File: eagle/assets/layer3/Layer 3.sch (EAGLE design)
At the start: 84 parts, among them Q2 AO3402, X1 SM06B-SRSS-TB, Y1 8MHz

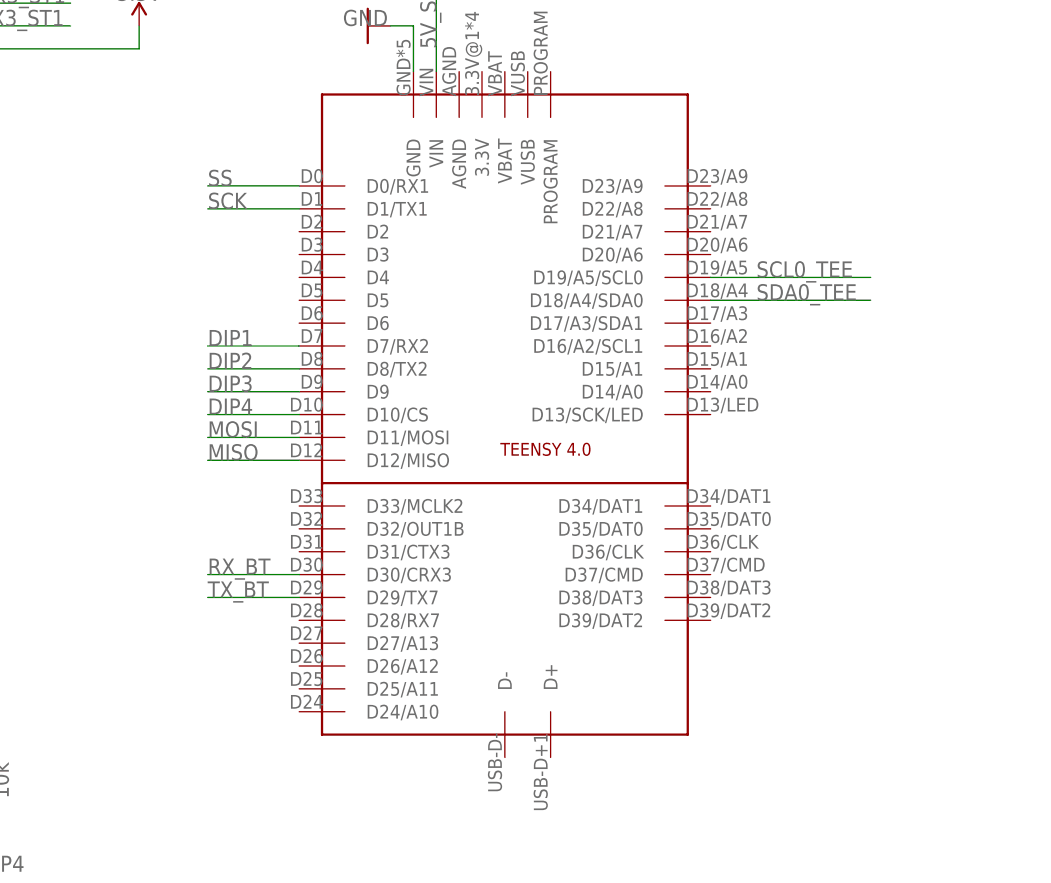
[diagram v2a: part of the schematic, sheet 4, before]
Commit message: final integration of teensy 4 to board
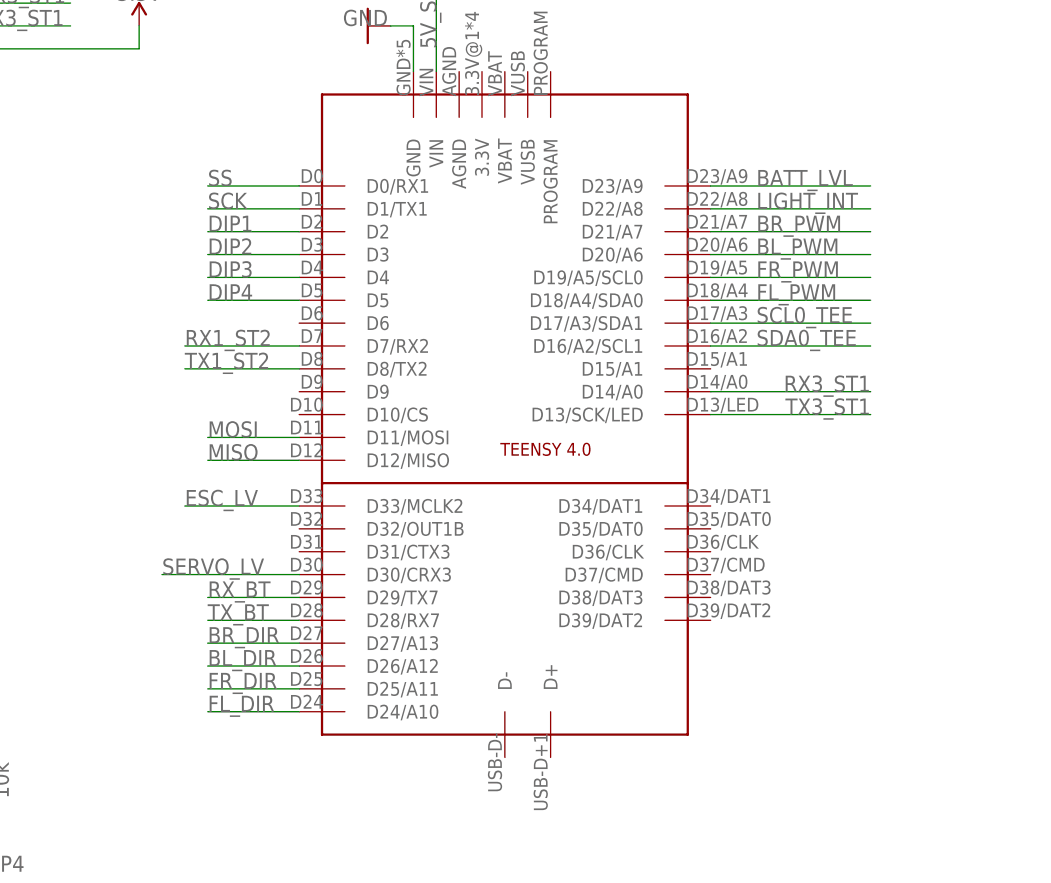
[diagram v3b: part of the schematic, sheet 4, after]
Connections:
- net BATT_LVL: now also U$1.D23/A9
- net BL_DIR: now also U$1.D26/A12
- net BL_PWM: now also U$1.D20/A6
- net BR_DIR: now also U$1.D27/A13
- net BR_PWM: now also U$1.D21/A7
- net DIP1: now also U$1.D2; no longer U$1.D7/RX2
- net DIP2: now also U$1.D3; no longer U$1.D8/TX2
- net DIP3: now also U$1.D4; no longer U$1.D9
- net DIP4: now also U$1.D5; no longer U$1.D10/CS
- net ESC_LV: now also U$1.D33/MCLK2
- net FL_DIR: now also U$1.D24/A10
- net FL_PWM: now also U$1.D18/A4/SDA0
- net FR_DIR: now also U$1.D25/A11
- net FR_PWM: now also U$1.D19/A5/SCL0
- net LIGHT_INT: now also U$1.D22/A8
- net RX1_ST2: now also U$1.D7/RX2
- net RX3_ST1: now also U$1.D14/A0
- net RX_BT: now also U$1.D29/TX7; no longer U$1.D30/CRX3
- net SCL0_TEE: now also U$1.D17/A3/SDA1; no longer U$1.D19/A5/SCL0
- net SDA0_TEE: now also U$1.D16/A2/SCL1; no longer U$1.D18/A4/SDA0
- net SERVO_LV: now also U$1.D30/CRX3
- net TX1_ST2: now also U$1.D8/TX2
- net TX3_ST1: now also U$1.D13/SCK/LED
- net TX_BT: now also U$1.D28/RX7; no longer U$1.D29/TX7
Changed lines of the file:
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@@
 <label x="48.26" y="154.94" size="1.778" layer="95"/>
+</segment>
+<segment>
+<pinref part="U$1" gate="G$1" pin="D24/A10"/>
+<wire x1="83.82" y1="66.04" x2="73.66" y2="66.04" width="0.1524" layer="91"/>
+<label x="73.66" y="66.04" size="1.778" layer="95"/>
 </segment>
 </net>
@@
 <label x="48.26" y="152.4" size="1.778" layer="95"/>
 </segment>
+<segment>
+<pinref part="U$1" gate="G$1" pin="D25/A11"/>
+<wire x1="83.82" y1="68.58" x2="73.66" y2="68.58" width="0.1524" layer="91"/>
+<label x="73.66" y="68.58" size="1.778" layer="95"/>
+</segment>
 </net>
 <net name="BL_DIR" class="0">
@@
 <label x="48.26" y="149.86" size="1.778" layer="95"/>
 </segment>
+<segment>
+<pinref part="U$1" gate="G$1" pin="D26/A12"/>
+<wire x1="83.82" y1="71.12" x2="73.66" y2="71.12" width="0.1524" layer="91"/>
+<label x="73.66" y="71.12" size="1.778" layer="95"/>
+</segment>
 </net>
 <net name="BR_DIR" class="0">
@@
 <label x="48.26" y="147.32" size="1.778" layer="95"/>
 </segment>
+<segment>
+<pinref part="U$1" gate="G$1" pin="D27/A13"/>
+<wire x1="83.82" y1="73.66" x2="73.66" y2="73.66" width="0.1524" layer="91"/>
+<label x="73.66" y="73.66" size="1.778" layer="95"/>
+</segment>
 </net>
 <net name="RX3_ST1" class="0">
@@
 <label x="48.26" y="144.78" size="1.778" layer="95"/>
 </segment>
+<segment>
+<wire x1="129.54" y1="101.6" x2="147.32" y2="101.6" width="0.1524" layer="91"/>
+<label x="147.32" y="103.378" size="1.778" layer="95" rot="R180"/>
+<pinref part="U$1" gate="G$1" pin="D14/A0"/>
+</segment>
 </net>
 <net name="TX3_ST1" class="0">
@@
 <wire x1="48.26" y1="142.24" x2="58.42" y2="142.24" width="0.1524" layer="91"/>
 <label x="48.26" y="142.24" size="1.778" layer="95"/>
+</segment>
+<segment>
+<wire x1="129.54" y1="99.06" x2="147.32" y2="99.06" width="0.1524" layer="91"/>
+<label x="147.32" y="100.838" size="1.778" layer="95" rot="R180"/>
+<pinref part="U$1" gate="G$1" pin="D13/SCK/LED"/>
 </segment>
 </net>
@@
 <label x="22.86" y="154.94" size="1.778" layer="95"/>
 </segment>
+<segment>
+<pinref part="U$1" gate="G$1" pin="D18/A4/SDA0"/>
+<wire x1="129.54" y1="111.76" x2="147.32" y2="111.76" width="0.1524" layer="91"/>
+<label x="134.62" y="111.76" size="1.778" layer="95"/>
+</segment>
 </net>
 <net name="FR_PWM" class="0">
@@
 <label x="22.86" y="152.4" size="1.778" layer="95"/>
 </segment>
+<segment>
+<pinref part="U$1" gate="G$1" pin="D19/A5/SCL0"/>
+<wire x1="129.54" y1="114.3" x2="147.32" y2="114.3" width="0.1524" layer="91"/>
+<label x="134.62" y="114.3" size="1.778" layer="95"/>
+</segment>
 </net>
 <net name="BL_PWM" class="0">
@@
 <label x="22.86" y="149.86" size="1.778" layer="95"/>
 </segment>
+<segment>
+<pinref part="U$1" gate="G$1" pin="D20/A6"/>
+<wire x1="129.54" y1="116.84" x2="147.32" y2="116.84" width="0.1524" layer="91"/>
+<label x="134.62" y="116.84" size="1.778" layer="95"/>
+</segment>
 </net>
 <net name="BR_PWM" class="0">
@@
 <label x="22.86" y="147.32" size="1.778" layer="95"/>
 </segment>
+<segment>
+<pinref part="U$1" gate="G$1" pin="D21/A7"/>
+<wire x1="129.54" y1="119.38" x2="147.32" y2="119.38" width="0.1524" layer="91"/>
+<label x="134.62" y="119.38" size="1.778" layer="95"/>
+</segment>
 </net>
 <net name="LIGHT_INT" class="0">
@@
 <label x="20.32" y="144.78" size="1.778" layer="95"/>
 </segment>
+<segment>
+<wire x1="129.54" y1="121.92" x2="147.32" y2="121.92" width="0.1524" layer="91"/>
+<label x="134.62" y="121.92" size="1.778" layer="95"/>
+<pinref part="U$1" gate="G$1" pin="D22/A8"/>
+</segment>
 </net>
 <net name="BATT_LVL" class="0">
@@
 <pinref part="U$14" gate="G$1" pin="11"/>
 <label x="20.32" y="142.24" size="1.778" layer="95"/>
+</segment>
+<segment>
+<wire x1="129.54" y1="124.46" x2="147.32" y2="124.46" width="0.1524" layer="91"/>
+<label x="134.62" y="124.46" size="1.778" layer="95"/>
+<pinref part="U$1" gate="G$1" pin="D23/A9"/>
 </segment>
 </net>
@@
 </segment>
 <segment>
-<pinref part="U$1" gate="G$1" pin="D18/A4/SDA0"/>
-<wire x1="129.54" y1="111.76" x2="147.32" y2="111.76" width="0.1524" layer="91"/>
-<label x="134.62" y="111.76" size="1.778" layer="95"/>
+<wire x1="129.54" y1="106.68" x2="147.32" y2="106.68" width="0.1524" layer="91"/>
+<label x="134.62" y="106.68" size="1.778" layer="95"/>
+<pinref part="U$1" gate="G$1" pin="D16/A2/SCL1"/>
 </segment>
 </net>
@@
 </segment>
 <segment>
-<pinref part="U$1" gate="G$1" pin="D19/A5/SCL0"/>
-<wire x1="129.54" y1="114.3" x2="147.32" y2="114.3" width="0.1524" layer="91"/>
-<label x="134.62" y="114.3" size="1.778" layer="95"/>
+<wire x1="129.54" y1="109.22" x2="147.32" y2="109.22" width="0.1524" layer="91"/>
+<label x="134.62" y="109.22" size="1.778" layer="95"/>
+<pinref part="U$1" gate="G$1" pin="D17/A3/SDA1"/>
 </segment>
 </net>
@@
 </segment>
 <segment>
-<wire x1="83.82" y1="106.68" x2="73.66" y2="106.68" width="0.1524" layer="91"/>
-<label x="73.66" y="106.68" size="1.778" layer="95"/>
-<pinref part="U$1" gate="G$1" pin="D7/RX2"/>
+<wire x1="83.82" y1="119.38" x2="73.66" y2="119.38" width="0.1524" layer="91"/>
+<label x="73.66" y="119.38" size="1.778" layer="95"/>
+<pinref part="U$1" gate="G$1" pin="D2"/>
 </segment>
 </net>
@@
 </segment>
 <segment>
-<wire x1="83.82" y1="104.14" x2="73.66" y2="104.14" width="0.1524" layer="91"/>
-<label x="73.66" y="104.14" size="1.778" layer="95"/>
-<pinref part="U$1" gate="G$1" pin="D8/TX2"/>
+<wire x1="83.82" y1="116.84" x2="73.66" y2="116.84" width="0.1524" layer="91"/>
+<label x="73.66" y="116.84" size="1.778" layer="95"/>
+<pinref part="U$1" gate="G$1" pin="D3"/>
 </segment>
 </net>
@@
 </segment>
 <segment>
-<wire x1="83.82" y1="101.6" x2="73.66" y2="101.6" width="0.1524" layer="91"/>
-<label x="73.66" y="101.6" size="1.778" layer="95"/>
-<pinref part="U$1" gate="G$1" pin="D9"/>
+<wire x1="83.82" y1="114.3" x2="73.66" y2="114.3" width="0.1524" layer="91"/>
+<label x="73.66" y="114.3" size="1.778" layer="95"/>
+<pinref part="U$1" gate="G$1" pin="D4"/>
 </segment>
 </net>
@@
 </segment>
 <segment>
-<wire x1="83.82" y1="99.06" x2="73.66" y2="99.06" width="0.1524" layer="91"/>
-<label x="73.66" y="99.06" size="1.778" layer="95"/>
-<pinref part="U$1" gate="G$1" pin="D10/CS"/>
+<wire x1="83.82" y1="111.76" x2="73.66" y2="111.76" width="0.1524" layer="91"/>
+<label x="73.66" y="111.76" size="1.778" layer="95"/>
+<pinref part="U$1" gate="G$1" pin="D5"/>
 </segment>
 </net>
@@
 </segment>
 <segment>
-<wire x1="83.82" y1="81.28" x2="73.66" y2="81.28" width="0.1524" layer="91"/>
-<label x="73.66" y="81.28" size="1.778" layer="95"/>
-<pinref part="U$1" gate="G$1" pin="D30/CRX3"/>
+<wire x1="83.82" y1="78.74" x2="73.66" y2="78.74" width="0.1524" layer="91"/>
+<label x="73.66" y="78.74" size="1.778" layer="95"/>
+<pinref part="U$1" gate="G$1" pin="D29/TX7"/>
 </segment>
 </net>
@@
 </segment>
 <segment>
-<wire x1="83.82" y1="78.74" x2="73.66" y2="78.74" width="0.1524" layer="91"/>
-<label x="73.66" y="78.74" size="1.778" layer="95"/>
-<pinref part="U$1" gate="G$1" pin="D29/TX7"/>
-</segment>
-</net>
+<wire x1="83.82" y1="76.2" x2="73.66" y2="76.2" width="0.1524" layer="91"/>
+<label x="73.66" y="76.2" size="1.778" layer="95"/>
+<pinref part="U$1" gate="G$1" pin="D28/RX7"/>
+</segment>
+</net>
+<net name="ESC_LV" class="0">
+<segment>
+<wire x1="83.82" y1="88.9" x2="71.12" y2="88.9" width="0.1524" layer="91"/>
+<label x="71.12" y="88.9" size="1.778" layer="95"/>
+<pinref part="U$1" gate="G$1" pin="D33/MCLK2"/>
+</segment>
+</net>
+<net name="SERVO_LV" class="0">
+<segment>
+<wire x1="83.82" y1="81.28" x2="68.58" y2="81.28" width="0.1524" layer="91"/>
+<label x="68.58" y="81.28" size="1.778" layer="95"/>
+<pinref part="U$1" gate="G$1" pin="D30/CRX3"/>
+</segment>
+</net>
+<net name="RX1_ST2" class="0">
+<segment>
+<wire x1="83.82" y1="106.68" x2="71.12" y2="106.68" width="0.1524" layer="91"/>
+<label x="71.12" y="106.68" size="1.778" layer="95"/>
+<pinref part="U$1" gate="G$1" pin="D7/RX2"/>
+</segment>
+</net>
+<net name="TX1_ST2" class="0">
+<segment>
+<wire x1="83.82" y1="104.14" x2="71.12" y2="104.14" width="0.1524" layer="91"/>
+<label x="71.12" y="104.14" size="1.778" layer="95"/>
+<pinref part="U$1" gate="G$1" pin="D8/TX2"/>
+</segment>
+</net>
